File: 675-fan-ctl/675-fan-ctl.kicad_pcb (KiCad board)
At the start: 2 copper layers, 44.6 x 39.4 mm, 15 parts, among them J1 +, J2 -, J3 M+, J4 M-, Q1 3055T, SW1 High Spin, U1 LM7805_TO220, U2 PIC12F675-IP

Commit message: small changes.
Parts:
- added J5: 2, Connectors:Pin_d1.4mm_L8.5mm_W2.8mm_FlatFork, F.Cu at (49.9, 61.4)
- added J6: Conn_01x01_Male, Connectors:Pin_d1.4mm_L8.5mm_W2.8mm_FlatFork, F.Cu at (59.9, 68.2)
- added REF**: MountingHole_2.5mm, Mounting_Holes:MountingHole_2.5mm, F.Cu at (78.3, 70.9)
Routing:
- net Net-(J6-Pad1): track 0.00 -> 12.2 mm
- net Net-(J5-Pad1): track 0.00 -> 9.84 mm
- net GND: track 124.3 -> 126.0 mm
- net Net-(C2-Pad1): track 37.8 -> 36.1 mm
- added copper zone on B.Cu, net (none)
- added copper zone on F.Cu, net (none)

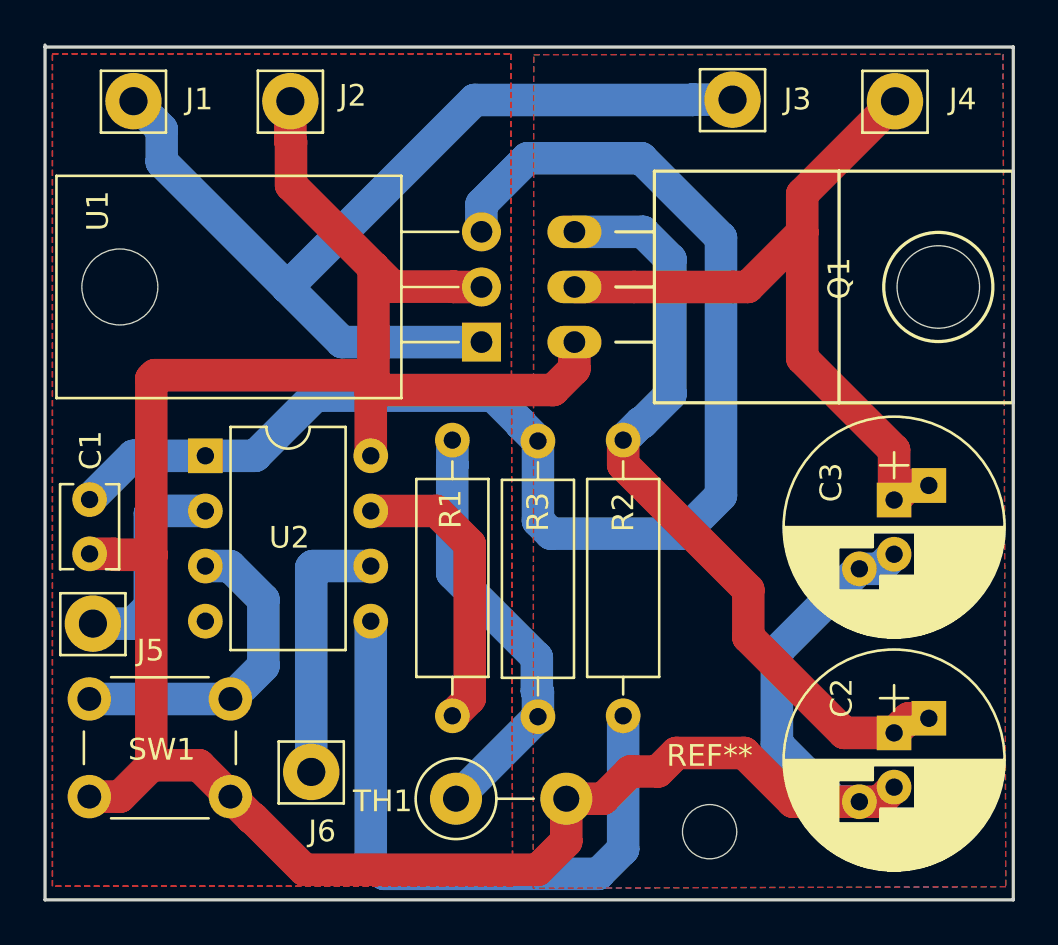
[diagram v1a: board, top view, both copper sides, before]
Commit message: add capacitor.
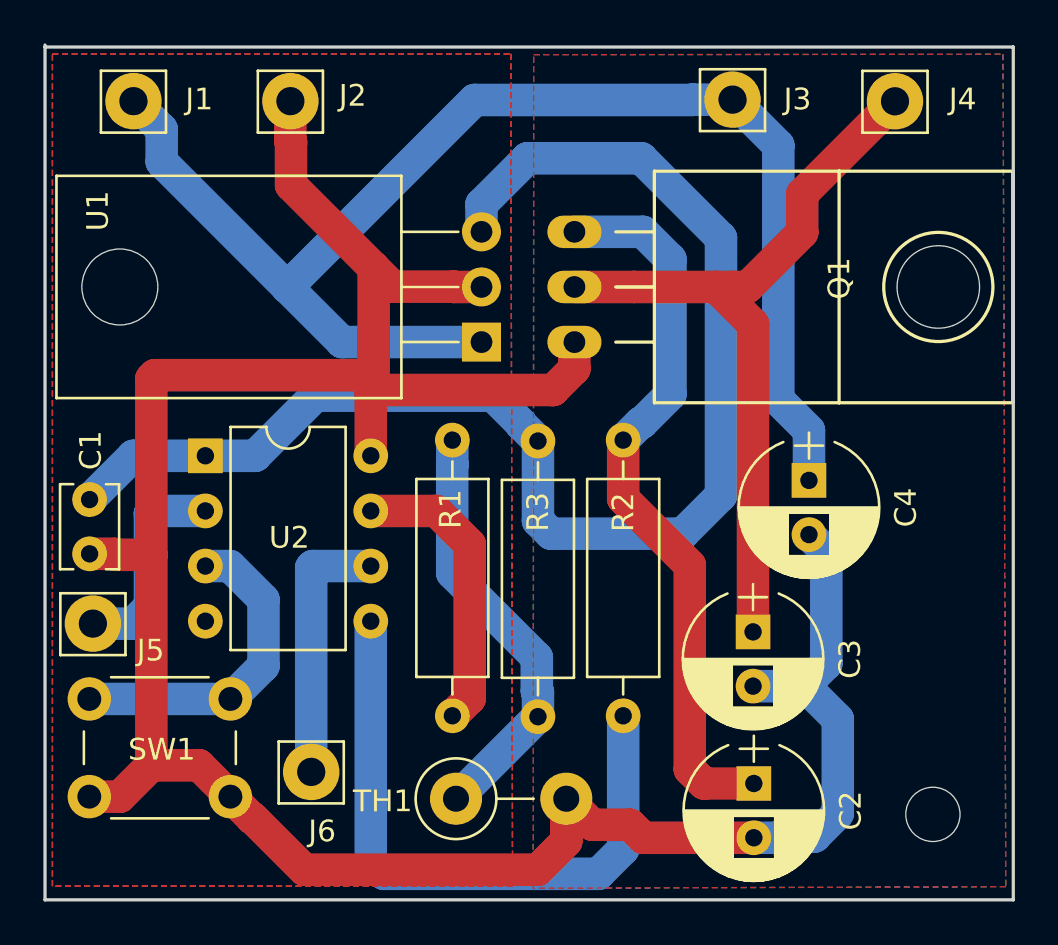
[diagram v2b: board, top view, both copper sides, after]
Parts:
- added C4: 47u, Capacitors_THT:CP_Radial_D6.3mm_P2.50mm, F.Cu at (82.9, 54.8)
- C2, C3: footprint Capacitors_THT:CP_Radial_D10.0mm_P2.50mm_P5.00mm -> Capacitors_THT:CP_Radial_D6.3mm_P2.50mm
- J5: value 2 -> Conn_01x01_Male
- moved REF** 10.3 mm to (88.6, 70.1)
- moved C3 8.90 mm to (80.3, 61.7)
- moved C2 6.87 mm to (80.3, 68.7)
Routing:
- net VCC: track 45.6 -> 64.6 mm
- net GND: track 126.0 -> 122.7 mm
- net Net-(C2-Pad1): track 36.1 -> 33.9 mm
- net Net-(C3-Pad1): track 35.3 -> 35.9 mm
